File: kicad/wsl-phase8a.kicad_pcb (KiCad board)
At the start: 2 copper layers, 100 x 100 mm, 60 parts, among them J1 5.08mm 2P TB, J10 5.08mm 2P TB, J11 5.08mm 2P TB, J2 5.08mm 2P TB, J3 5.08mm 2P TB, J4 5.08mm 2P TB, J5 5.08mm 2P TB, J6 5.08mm 2P TB, J7 5.08mm 2P TB, J8 5.08mm 2P TB, J9 5.08mm 2P TB, Q1 AO3400A, Q2 AO3400A, U1 NE555

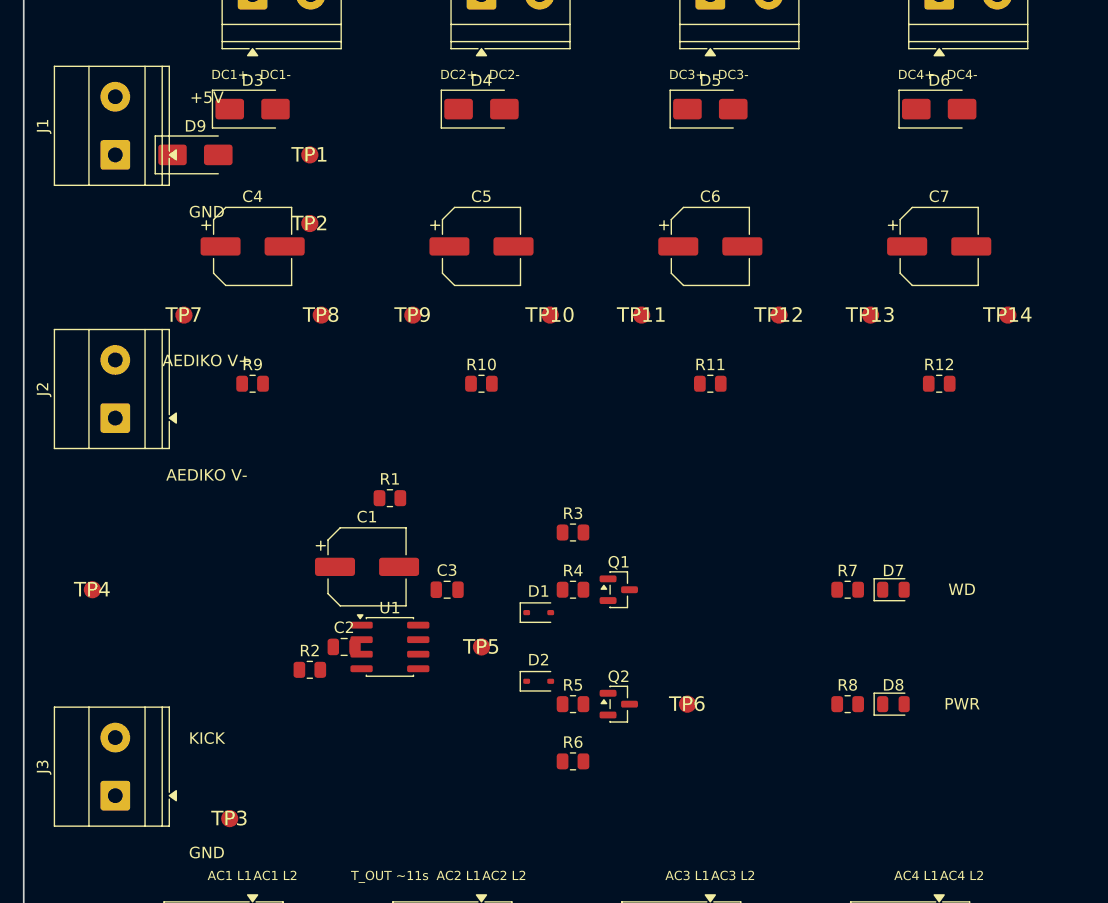
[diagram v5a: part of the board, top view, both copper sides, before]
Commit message: Fix diode polarity + AC channel pad alignment per Codex pre-route audit
Codex caught D9 backwards. Verified via .kicad_pcb inspection: at
rotation 0, KiCad's Diode_SMD:D_SMA puts pin 1 (K) on the LEFT. With
D9 at (15, 22, 0), K was facing J1 (wrong — that's the raw supply
side, should be the anode). Trace from J1.1 to D9.A would have had to
detour around D9's body.

Three rotation fixes applied:

1. D9 (SS14) rotation 0 -> 180: anode now on LEFT toward J1.1, cathode
   on RIGHT toward VCC_5V loads. VCC_5V_RAW becomes a straight ~5mm
   horizontal stub from J1 to D9.A.

2. D1, D2 (diode-OR isolation) rotation 0 -> 180: anodes (pin 2) now
   on LEFT toward U1.7/U1.2 (TIMING_NODE/TRIG, the noise-sensitive
   nets per Codex), cathodes (pin 1) on RIGHT toward Q1_DRAIN. Cuts
   the critical TIMING_NODE trace from ~14mm to ~10mm.

3. D3-D6, C4-C7, R9-R12 rotation 0 -> 90: all AC channel components
   rotated 90° so their pads align with the vertical column trace
   (pin 1 at top, pin 2 at bottom). Diode K at top toward DC_OUT,
   cap + at top toward DC_POS. AC channel columns are now truly
   vertical end-to-end.

Also moved U1 from (32, 65) to (32, 66): adds ~1mm of courtyard
clearance to C1 (which sits at y=58, 6.3mm diameter body extends
to y=61.15; U1 courtyard top was at y=62.5, gap 1.35mm; now 2.35mm).

Co-Authored-By: Claude Opus 4.7 (1M context) <noreply@anthropic.com>
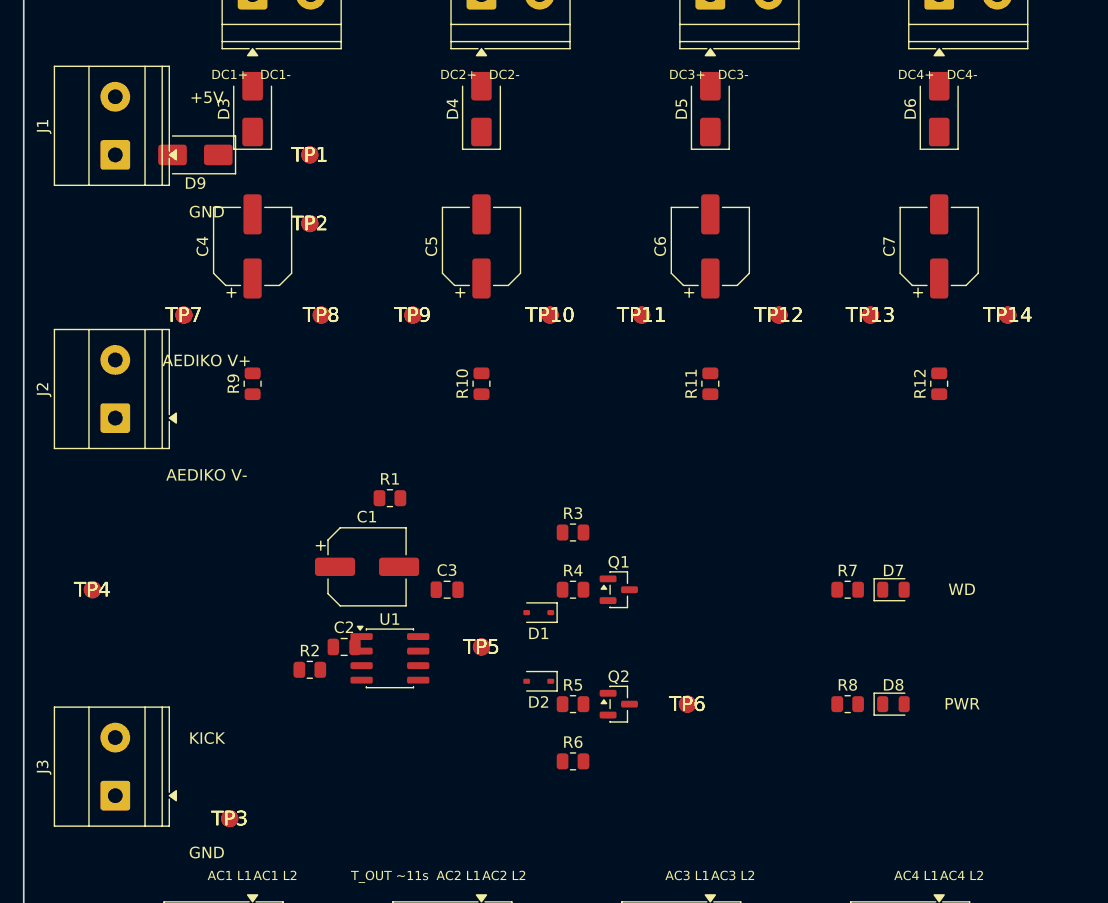
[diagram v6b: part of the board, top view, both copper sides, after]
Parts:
- removed the TP1 at (25.0, 22.0)
- removed the TP10 at (46.0, 36.0)
- removed the TP11 at (54.0, 36.0)
- removed the TP12 at (66.0, 36.0)
- removed the TP13 at (74.0, 36.0)
- removed the TP14 at (86.0, 36.0)
- removed the TP2 at (25.0, 28.0)
- removed the TP3 at (18.0, 80.0)
- removed the TP4 at (6.00, 60.0)
- removed the TP5 at (40.0, 65.0)
- removed the TP6 at (58.0, 70.0)
- removed the TP7 at (14.0, 36.0)
- removed the TP8 at (26.0, 36.0)
- removed the TP9 at (34.0, 36.0)
- added TP1 (x2): VCC_5V, , F.Cu at (25.0, 22.0)
- added TP10 (x2): CH2_RETURN, , F.Cu at (46.0, 36.0)
- added TP11 (x2): DC_CH3_POS, , F.Cu at (54.0, 36.0)
- added TP12 (x2): CH3_RETURN, , F.Cu at (66.0, 36.0)
- added TP13 (x2): DC_CH4_POS, , F.Cu at (74.0, 36.0)
- added TP14 (x2): CH4_RETURN, , F.Cu at (86.0, 36.0)
- added TP2 (x2): GND, , F.Cu at (25.0, 28.0)
- added TP3 (x2): KICK, , F.Cu at (18.0, 80.0)
- added TP4 (x2): TIMING_NODE, , F.Cu at (6.00, 60.0)
- added TP5 (x2): NE555_OUT, , F.Cu at (40.0, 65.0)
- added TP6 (x2): COIL_GND_RETURN, , F.Cu at (58.0, 70.0)
- added TP7 (x2): DC_CH1_POS, , F.Cu at (14.0, 36.0)
- added TP8 (x2): CH1_RETURN, , F.Cu at (26.0, 36.0)
- added TP9 (x2): DC_CH2_POS, , F.Cu at (34.0, 36.0)
- moved U1 1.00 mm to (32.0, 66.0)
- turned C4 to 90 degrees
- turned C5 to 90 degrees
- turned C6 to 90 degrees
- turned C7 to 90 degrees
- turned D1 to 180 degrees
- turned D2 to 180 degrees
- turned D3 to 90 degrees
- turned D4 to 90 degrees
- turned D5 to 90 degrees
- turned D6 to 90 degrees
- turned D9 to 180 degrees
- turned R10 to 90 degrees
- turned R11 to 90 degrees
- turned R12 to 90 degrees
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
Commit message: Add B.Cu keepout zones to force AC channel isolation
Codex post-route audit caught FreeRouting taking shortcuts: CH1/CH2
return nets routed on bottom layer (B.Cu) through the watchdog area
rather than staying in their channel columns. Class-specific keepouts
require KiCad custom rules (.kicad_dru) DSL which is complex; instead
applied generic B.Cu keepouts in the 5 gap regions between channel
columns (x=14-18, 23-37, 43-57, 63-77, 83-92, y=5-95). This blocks
bottom-layer routing in those gaps, forcing AC returns to stay in
their channel columns. F.Cu is unaffected so watchdog routes
(predominantly on top layer) continue normally.

Two KiCad 10 API quirks discovered while writing this:
- ZONE.SetDoNotAllowCopperPour renamed to SetDoNotAllowZoneFills
- SHAPE_POLY_SET.Fix() removed; polygons now auto-close

Co-Authored-By: Claude Opus 4.7 (1M context) <noreply@anthropic.com>
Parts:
- removed the TP1 at (25.0, 22.0) (x2)
- removed the TP10 at (46.0, 36.0) (x2)
- removed the TP11 at (54.0, 36.0) (x2)
- removed the TP12 at (66.0, 36.0) (x2)
- removed the TP13 at (74.0, 36.0) (x2)
- removed the TP14 at (86.0, 36.0) (x2)
- removed the TP2 at (25.0, 28.0) (x2)
- removed the TP3 at (18.0, 80.0) (x2)
- removed the TP4 at (6.00, 60.0) (x2)
- removed the TP5 at (40.0, 65.0) (x2)
- removed the TP6 at (58.0, 70.0) (x2)
- removed the TP7 at (14.0, 36.0) (x2)
- removed the TP8 at (26.0, 36.0) (x2)
- removed the TP9 at (34.0, 36.0) (x2)
- added TP1 (x2): VCC_5V, , F.Cu at (25.0, 22.0)
- added TP10 (x2): CH2_RETURN, , F.Cu at (46.0, 36.0)
- added TP11 (x2): DC_CH3_POS, , F.Cu at (54.0, 36.0)
- added TP12 (x2): CH3_RETURN, , F.Cu at (66.0, 36.0)
- added TP13 (x2): DC_CH4_POS, , F.Cu at (74.0, 36.0)
- added TP14 (x2): CH4_RETURN, , F.Cu at (86.0, 36.0)
- added TP2 (x2): GND, , F.Cu at (25.0, 28.0)
- added TP3 (x2): KICK, , F.Cu at (18.0, 80.0)
- added TP4 (x2): TIMING_NODE, , F.Cu at (6.00, 60.0)
- added TP5 (x2): NE555_OUT, , F.Cu at (40.0, 65.0)
- added TP6 (x2): COIL_GND_RETURN, , F.Cu at (58.0, 70.0)
- added TP7 (x2): DC_CH1_POS, , F.Cu at (14.0, 36.0)
- added TP8 (x2): CH1_RETURN, , F.Cu at (26.0, 36.0)
- added TP9 (x2): DC_CH2_POS, , F.Cu at (34.0, 36.0)

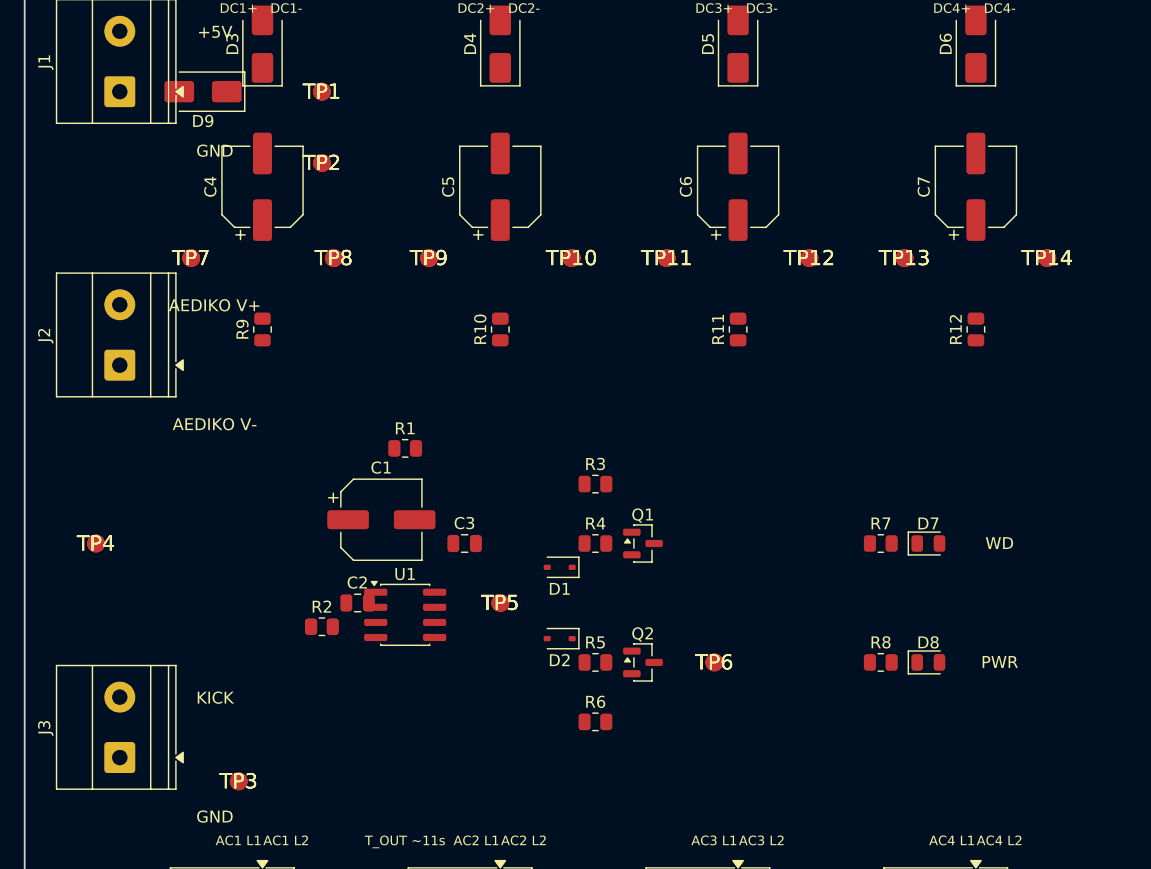
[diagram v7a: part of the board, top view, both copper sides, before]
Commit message: Fix DRC clearance errors: move C2 and D9 to clear courtyard overlaps
DRC report from first routed rev surfaced 5 real errors:
- C2.pad2 (GND) at (28.95, 65.0) was 0.7mm from U1.pad2 (TRIG) at
  (29.525, 65.365), causing shorting + solder-mask-bridge violations.
  C2 moved 4mm left to (24, 65). Pads now 4.6mm apart.
- D9 at (15, 22) had courtyard overlaps with both J1 (body x=2-14)
  AND channel-1 D3 at (20, 18). Moved DOWN to (10, 35) — in the gap
  between J1 and J2 vertically, at x=10 OUTSIDE the gap_J1_to_ch1
  B.Cu keepout (which starts at x=14). VCC_5V_RAW trace is ~13mm
  diagonal from J1.1 to D9.A, still short.
- Unconnected NE555_TRIG pin should re-route cleanly after the C2
  move opens up the area around U1.

97 cosmetic silkscreen warnings remain (test pad refdes overlapping
their own pad, AC label overlaps, etc.) — those don't affect fab.

Co-Authored-By: Claude Opus 4.7 (1M context) <noreply@anthropic.com>
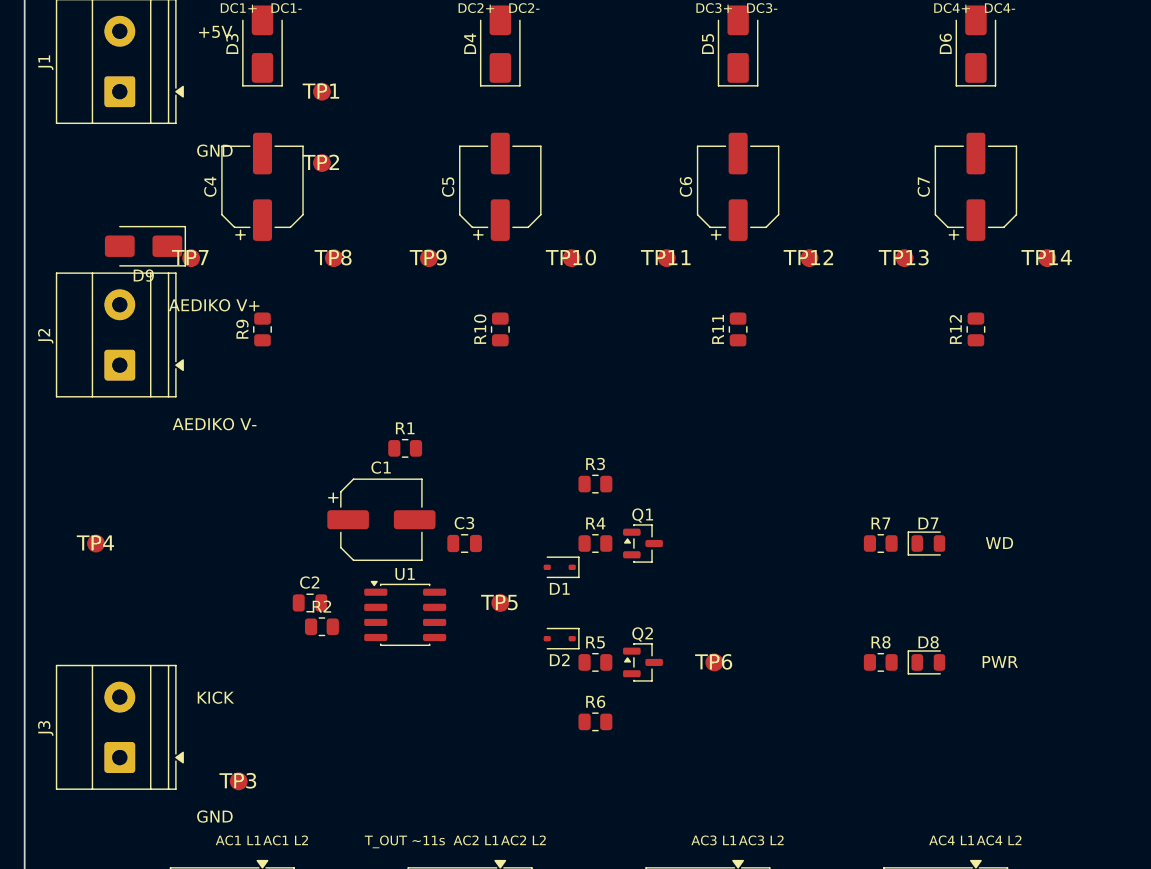
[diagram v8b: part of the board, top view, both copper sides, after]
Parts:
- removed the TP1 at (25.0, 22.0) (x2)
- removed the TP10 at (46.0, 36.0) (x2)
- removed the TP11 at (54.0, 36.0) (x2)
- removed the TP12 at (66.0, 36.0) (x2)
- removed the TP13 at (74.0, 36.0) (x2)
- removed the TP14 at (86.0, 36.0) (x2)
- removed the TP2 at (25.0, 28.0) (x2)
- removed the TP3 at (18.0, 80.0) (x2)
- removed the TP4 at (6.00, 60.0) (x2)
- removed the TP5 at (40.0, 65.0) (x2)
- removed the TP6 at (58.0, 70.0) (x2)
- removed the TP7 at (14.0, 36.0) (x2)
- removed the TP8 at (26.0, 36.0) (x2)
- removed the TP9 at (34.0, 36.0) (x2)
- added TP1: VCC_5V, custom:test_pad_1.5mm, F.Cu at (25.0, 22.0)
- added TP10: CH2_RETURN, custom:test_pad_1.5mm, F.Cu at (46.0, 36.0)
- added TP11: DC_CH3_POS, custom:test_pad_1.5mm, F.Cu at (54.0, 36.0)
- added TP12: CH3_RETURN, custom:test_pad_1.5mm, F.Cu at (66.0, 36.0)
- added TP13: DC_CH4_POS, custom:test_pad_1.5mm, F.Cu at (74.0, 36.0)
- added TP14: CH4_RETURN, custom:test_pad_1.5mm, F.Cu at (86.0, 36.0)
- added TP2: GND, custom:test_pad_1.5mm, F.Cu at (25.0, 28.0)
- added TP3: KICK, custom:test_pad_1.5mm, F.Cu at (18.0, 80.0)
- added TP4: TIMING_NODE, custom:test_pad_1.5mm, F.Cu at (6.00, 60.0)
- added TP5: NE555_OUT, custom:test_pad_1.5mm, F.Cu at (40.0, 65.0)
- added TP6: COIL_GND_RETURN, custom:test_pad_1.5mm, F.Cu at (58.0, 70.0)
- added TP7: DC_CH1_POS, custom:test_pad_1.5mm, F.Cu at (14.0, 36.0)
- added TP8: CH1_RETURN, custom:test_pad_1.5mm, F.Cu at (26.0, 36.0)
- added TP9: DC_CH2_POS, custom:test_pad_1.5mm, F.Cu at (34.0, 36.0)
- moved D9 13.9 mm to (10.0, 35.0)
- moved C2 4.00 mm to (24.0, 65.0)
